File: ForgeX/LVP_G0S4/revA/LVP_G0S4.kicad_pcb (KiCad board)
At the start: 2 copper layers, 159.9 x 47.5 mm, 74 parts, among them J1 Conn_02x05_Odd_Even, J10 Conn_01x02_Pin, J11 Conn_01x02_Pin, J12 Conn_01x02_Pin, J13 Conn_01x02_Pin, J14 Conn_02x05_Odd_Even, J16 Conn_01x04, J17 Conn_01x04, J2 Conn_02x05_Odd_Even, J3 Conn_02x05_Odd_Even, J4 Conn_02x05_Odd_Even, J5 Conn_01x04_Pin, J6 Conn_02x20_Odd_Even, J7 Conn_01x02_Pin, J8 Conn_01x02_Pin, J9 Screw_Terminal_01x09, Q2 AO3400A, U1 SP485EEN-TD, U2 SP485EEN-TD, U3 SP485EEN-TD, U4 AMS1117-3.3, U5 LM311, U6 LM311, U7 LM311

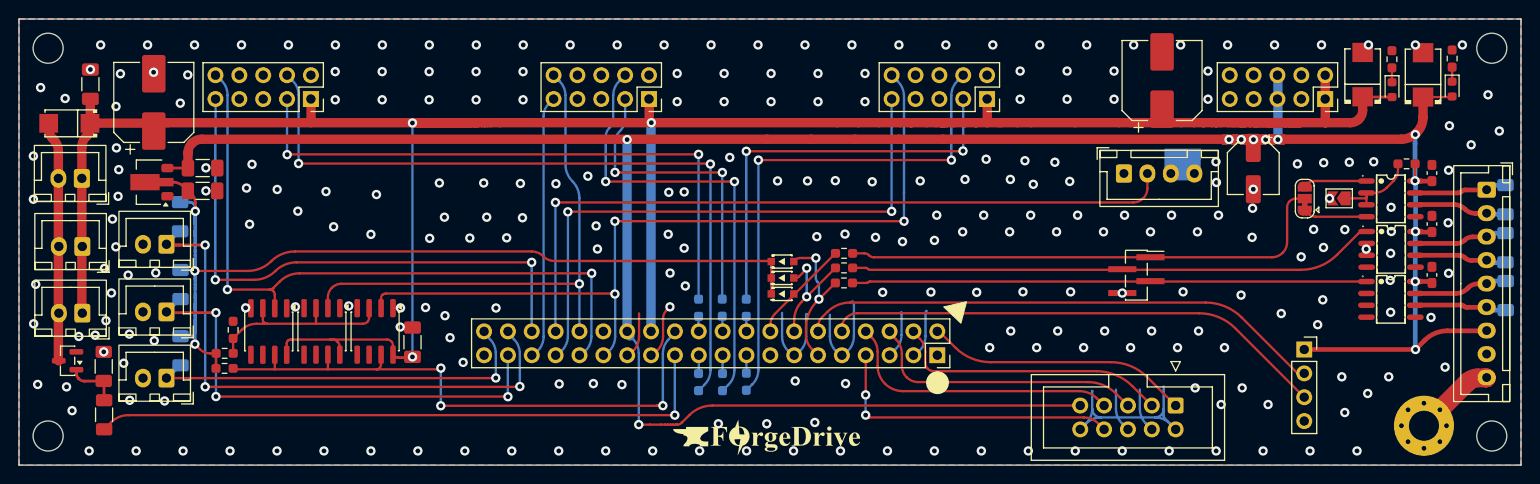
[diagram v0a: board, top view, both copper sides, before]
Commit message: LVP OCP comparators removal
Initiallly put for short circuit protection, and quick analysis reveals they are not fit for the use case , and add complexity there , OCP can be included in HBM much better or in MGD's
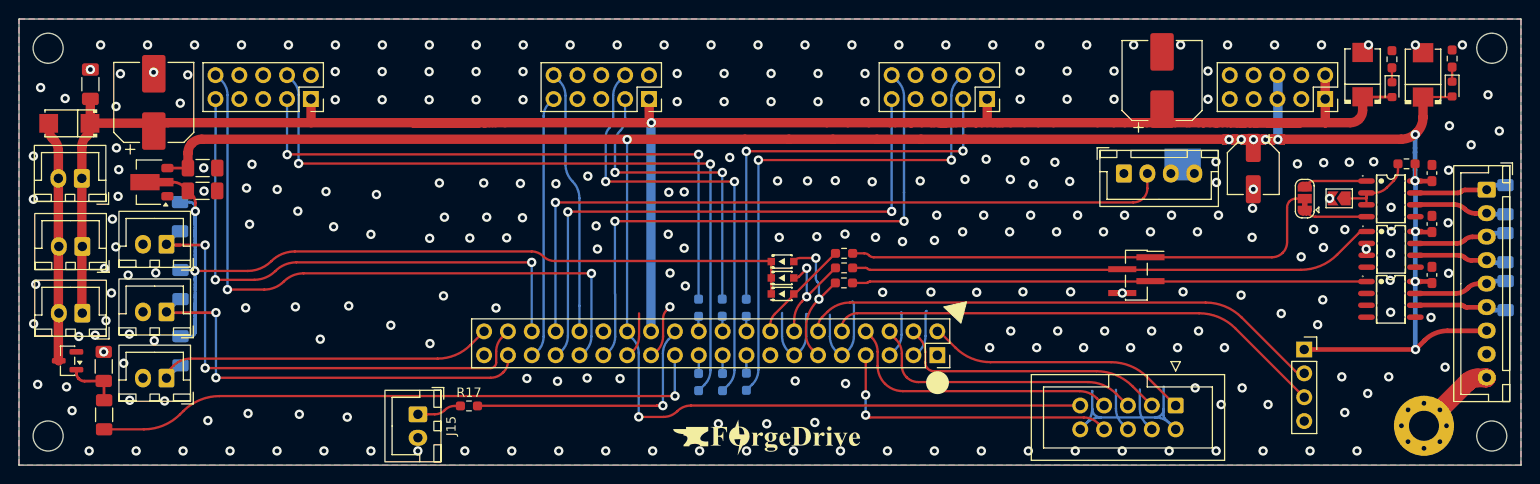
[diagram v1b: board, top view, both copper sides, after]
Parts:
- removed C7: 0.1u, Capacitor_SMD:C_1206_3216Metric_Pad1.33x1.80mm_HandSolder
- removed R18: 10k, Resistor_SMD:R_0603_1608Metric_Pad0.98x0.95mm_HandSolder
- removed R21: 330, Resistor_SMD:R_0603_1608Metric_Pad0.98x0.95mm_HandSolder
- removed U5, U6, U7: LM311, Package_SO:SOIC-8_3.9x4.9mm_P1.27mm
- added J15: Conn_01x02_Pin, Connector_JST:JST_XH_B2B-XH-A_1x02_P2.50mm_Vertical, F.Cu at (103.4, 100.4)
- moved R17 26.6 mm to (108.8, 99.5), turned to 0 degrees
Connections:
- R17 pad 2: +3.3V -> /~{BKIN}
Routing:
- net +12V: track 242.4 -> 198.1 mm, vias 3 -> 1
- net /~{BKIN}: track 62.9 -> 27.9 mm, vias 3 -> 1
- net /Csense_{B}: track 57.0 -> 28.3 mm, vias 1 -> 0
- net /Csense_{A}: track 87.8 -> 61.7 mm, vias 3 -> 2
- net Net-(J15-Pin_1): track 21.7 -> 4.75 mm
- net /TEMP1: track 62.4 -> 55.8 mm, vias 3 -> 2
- net +3.3V: track 94.9 -> 88.9 mm, vias 3 -> 2
- net /TEMP2: track 51.6 -> 47.0 mm, vias 3 -> 2
- net /TEMP3: track 42.3 -> 37.9 mm, vias 1 -> 0
- net /Csense_{C}: track 75.1 -> 71.7 mm
- net /FAN0: track 67.5 -> 65.9 mm
- net +5V: track 278.1 -> 276.9 mm
- net GND: vias 258 -> 262

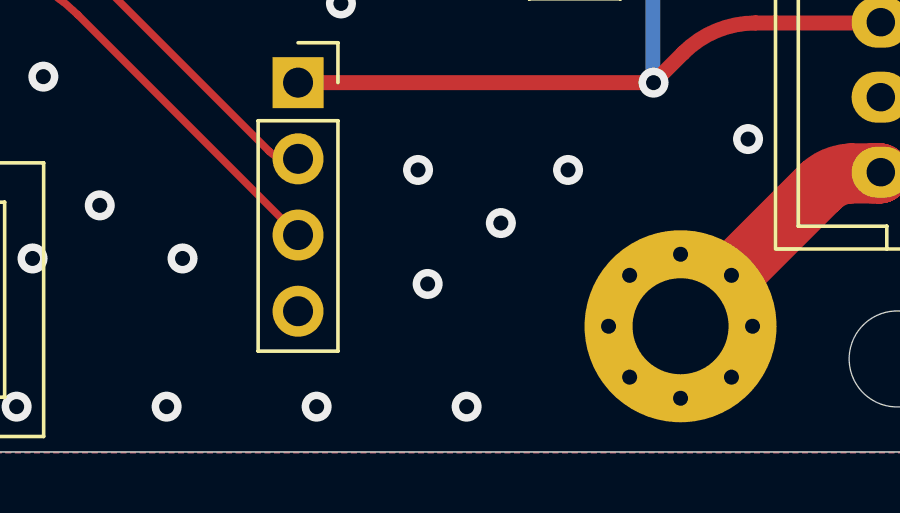
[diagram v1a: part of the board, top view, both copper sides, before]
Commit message: LVP_G0S4B variant from LVP_G0S4 for Ebikes
Added an LVP_G0S4B variant
(swapped temperature sensor 3 , for analog throttle & differential encoder phy interface to single ended encoders)
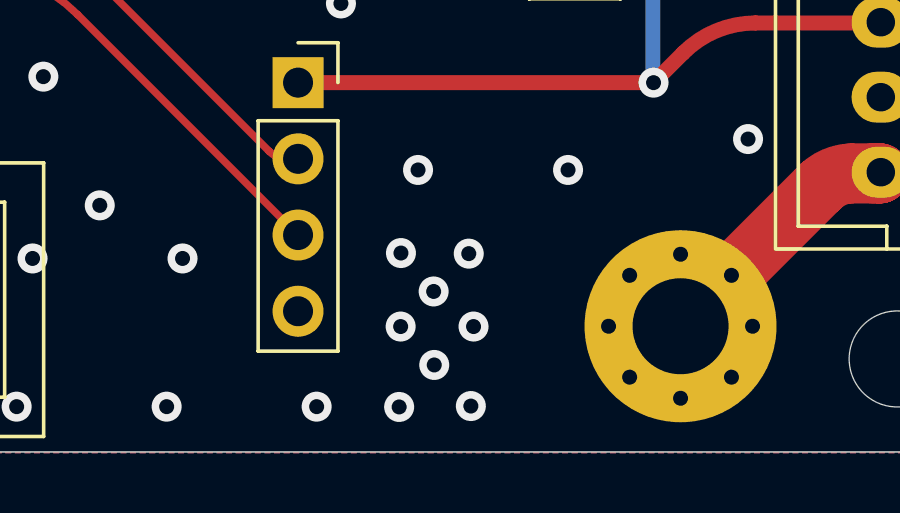
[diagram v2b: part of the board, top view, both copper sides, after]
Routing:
- net GND: vias 262 -> 267
